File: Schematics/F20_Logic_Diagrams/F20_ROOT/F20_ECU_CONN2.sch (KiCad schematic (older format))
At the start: 1 part, among them U5 ECU_Conn2

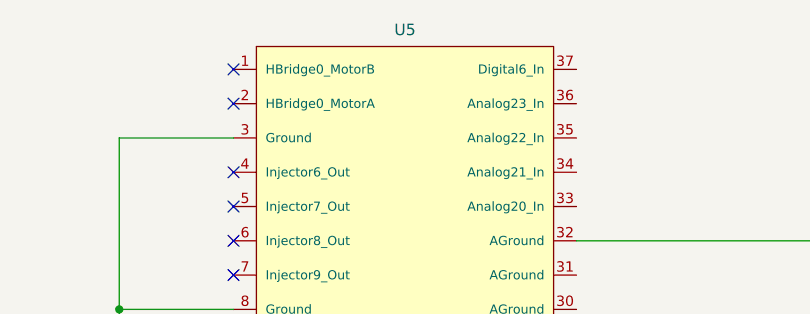
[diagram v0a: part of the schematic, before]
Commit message: Re-annotated Logic Diagrams, pulled a BOM list based on Logic Diagrams
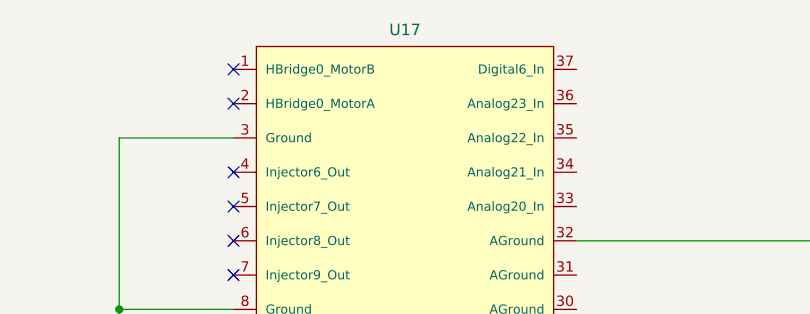
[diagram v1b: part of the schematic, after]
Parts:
- renumbered U5 to U17
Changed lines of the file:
@@
 $EndDescr
 $Comp
-L FSAE_Library:ECU_Conn2 U5
+L FSAE_Library:ECU_Conn2 U17
 U 1 1 5E5CA8D7
 P 4500 1500
-F 0 "U5" H 5250 1673 50  0000 C CNN
+F 0 "U17" H 5250 1673 50  0000 C CNN
 F 1 "ECU_Conn2" H 5250 1650 50  0001 C CNN
 F 2 "" H 5000 2500 50  0001 C CNN
@@
 Connection ~ 6500 3150
 $Comp
-L FSAE_Library:GND_BAT #PWR06
+L FSAE_Library:GND_BAT #PWR012
 U 1 1 5E5E871D
 P 6500 6000
-F 0 "#PWR06" H 6500 5750 50  0001 C CNN
+F 0 "#PWR012" H 6500 5750 50  0001 C CNN
 F 1 "GND_BAT" H 6505 5827 50  0000 C CNN
 F 2 "" H 6500 6000 50  0001 C CNN
@@
 	4000 1800 4000 2550
 $Comp
-L FSAE_Library:GND_BAT #PWR05
+L FSAE_Library:GND_BAT #PWR011
 U 1 1 5E5EE69E
 P 4000 6000
-F 0 "#PWR05" H 4000 5750 50  0001 C CNN
+F 0 "#PWR011" H 4000 5750 50  0001 C CNN
 F 1 "GND_BAT" H 4005 5827 50  0000 C CNN
 F 2 "" H 4000 6000 50  0001 C CNN
